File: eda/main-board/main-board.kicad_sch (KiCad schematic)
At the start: 11 parts, among them J3 Expansion, J4 $1-3 latch, J5 PWR, U1 W65C02SxP, X1 4Mhz

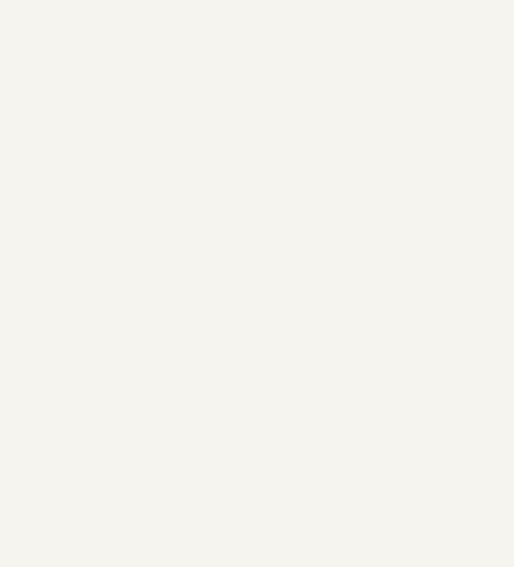
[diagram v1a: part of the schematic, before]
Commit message: Add expansion backplane
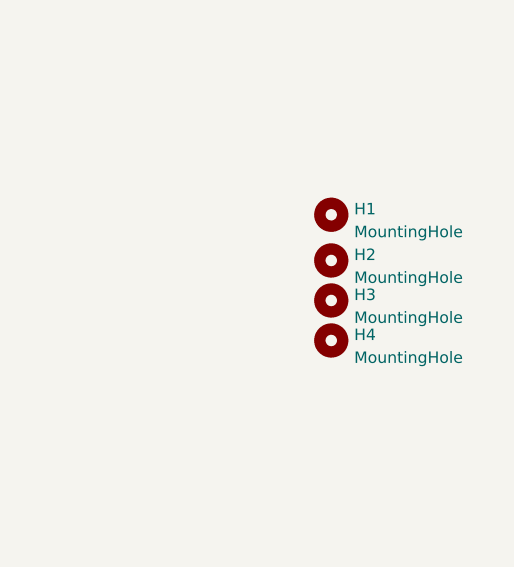
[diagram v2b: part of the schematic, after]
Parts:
- added H1, H2, H3, H4: MountingHole, MountingHole:MountingHole_2.1mm, symbol Mechanical:MountingHole
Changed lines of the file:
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@@
+    )
+  )
+  (symbol (lib_id "Mechanical:MountingHole") (at 267.97 137.16 0) (unit 1)
+    (in_bom yes) (on_board yes) (dnp no) (fields_autoplaced)
+    (property "Reference" "H1" (at 270.51 136.525 0)
+      (effects (font (size 1.27 1.27)) (justify left))
+    )
+    (property "Value" "MountingHole" (at 270.51 139.065 0)
+      (effects (font (size 1.27 1.27)) (justify left))
+    )
+    (property "Footprint" "MountingHole:MountingHole_2.1mm" (at 267.97 137.16 0)
+      (effects (font (size 1.27 1.27)) hide)
+    )
+    (property "Datasheet" "~" (at 267.97 137.16 0)
+      (effects (font (size 1.27 1.27)) hide)
+    )
+    (instances
+      (project "main-board"
+        (path "/2957ffac-6a43-4af7-8ab7-5cc1dbf2f2d7"
+          (reference "H1") (unit 1)
+        )
+      )
     )
   )
@@
     )
   )
+  (symbol (lib_id "Mechanical:MountingHole") (at 267.97 151.13 0) (unit 1)
+    (in_bom yes) (on_board yes) (dnp no) (fields_autoplaced)
+    (property "Reference" "H4" (at 270.51 150.495 0)
+      (effects (font (size 1.27 1.27)) (justify left))
+    )
+    (property "Value" "MountingHole" (at 270.51 153.035 0)
+      (effects (font (size 1.27 1.27)) (justify left))
+    )
+    (property "Footprint" "MountingHole:MountingHole_2.1mm" (at 267.97 151.13 0)
+      (effects (font (size 1.27 1.27)) hide)
+    )
+    (property "Datasheet" "~" (at 267.97 151.13 0)
+      (effects (font (size 1.27 1.27)) hide)
+    )
+    (instances
+      (project "main-board"
+        (path "/2957ffac-6a43-4af7-8ab7-5cc1dbf2f2d7"
+          (reference "H4") (unit 1)
+        )
+      )
+    )
+  )
   (symbol (lib_id "Device:R") (at 95.25 100.33 0) (unit 1)
     (in_bom yes) (on_board yes) (dnp no) (fields_autoplaced)
@@
     )
   )
+  (symbol (lib_id "Mechanical:MountingHole") (at 267.97 142.24 0) (unit 1)
+    (in_bom yes) (on_board yes) (dnp no) (fields_autoplaced)
+    (property "Reference" "H2" (at 270.51 141.605 0)
+      (effects (font (size 1.27 1.27)) (justify left))
+    )
+    (property "Value" "MountingHole" (at 270.51 144.145 0)
+      (effects (font (size 1.27 1.27)) (justify left))
+    )
+    (property "Footprint" "MountingHole:MountingHole_2.1mm" (at 267.97 142.24 0)
+      (effects (font (size 1.27 1.27)) hide)
+    )
+    (property "Datasheet" "~" (at 267.97 142.24 0)
+      (effects (font (size 1.27 1.27)) hide)
+    )
+    (instances
+      (project "main-board"
+        (path "/2957ffac-6a43-4af7-8ab7-5cc1dbf2f2d7"
+          (reference "H2") (unit 1)
+        )
+      )
+    )
+  )
   (symbol (lib_id "Device:R") (at 88.9 100.33 0) (unit 1)
     (in_bom yes) (on_board yes) (dnp no) (fields_autoplaced)
@@
         )
       )
+    )
+  )
+  (symbol (lib_id "Mechanical:MountingHole") (at 267.97 146.685 0) (unit 1)
+    (in_bom yes) (on_board yes) (dnp no) (fields_autoplaced)
+    (property "Reference" "H3" (at 270.51 146.05 0)
+      (effects (font (size 1.27 1.27)) (justify left))
+    )
+    (property "Value" "MountingHole" (at 270.51 148.59 0)
+      (effects (font (size 1.27 1.27)) (justify left))
+    )
+    (property "Footprint" "MountingHole:MountingHole_2.1mm" (at 267.97 146.685 0)
+      (effects (font (size 1.27 1.27)) hide)
+    )
+    (property "Datasheet" "~" (at 267.97 146.685 0)
+      (effects (font (size 1.27 1.27)) hide)
+    )
+    (instances
+      (project "main-board"
+        (path "/2957ffac-6a43-4af7-8ab7-5cc1dbf2f2d7"
+          (reference "H3") (unit 1)
+        )
+      )

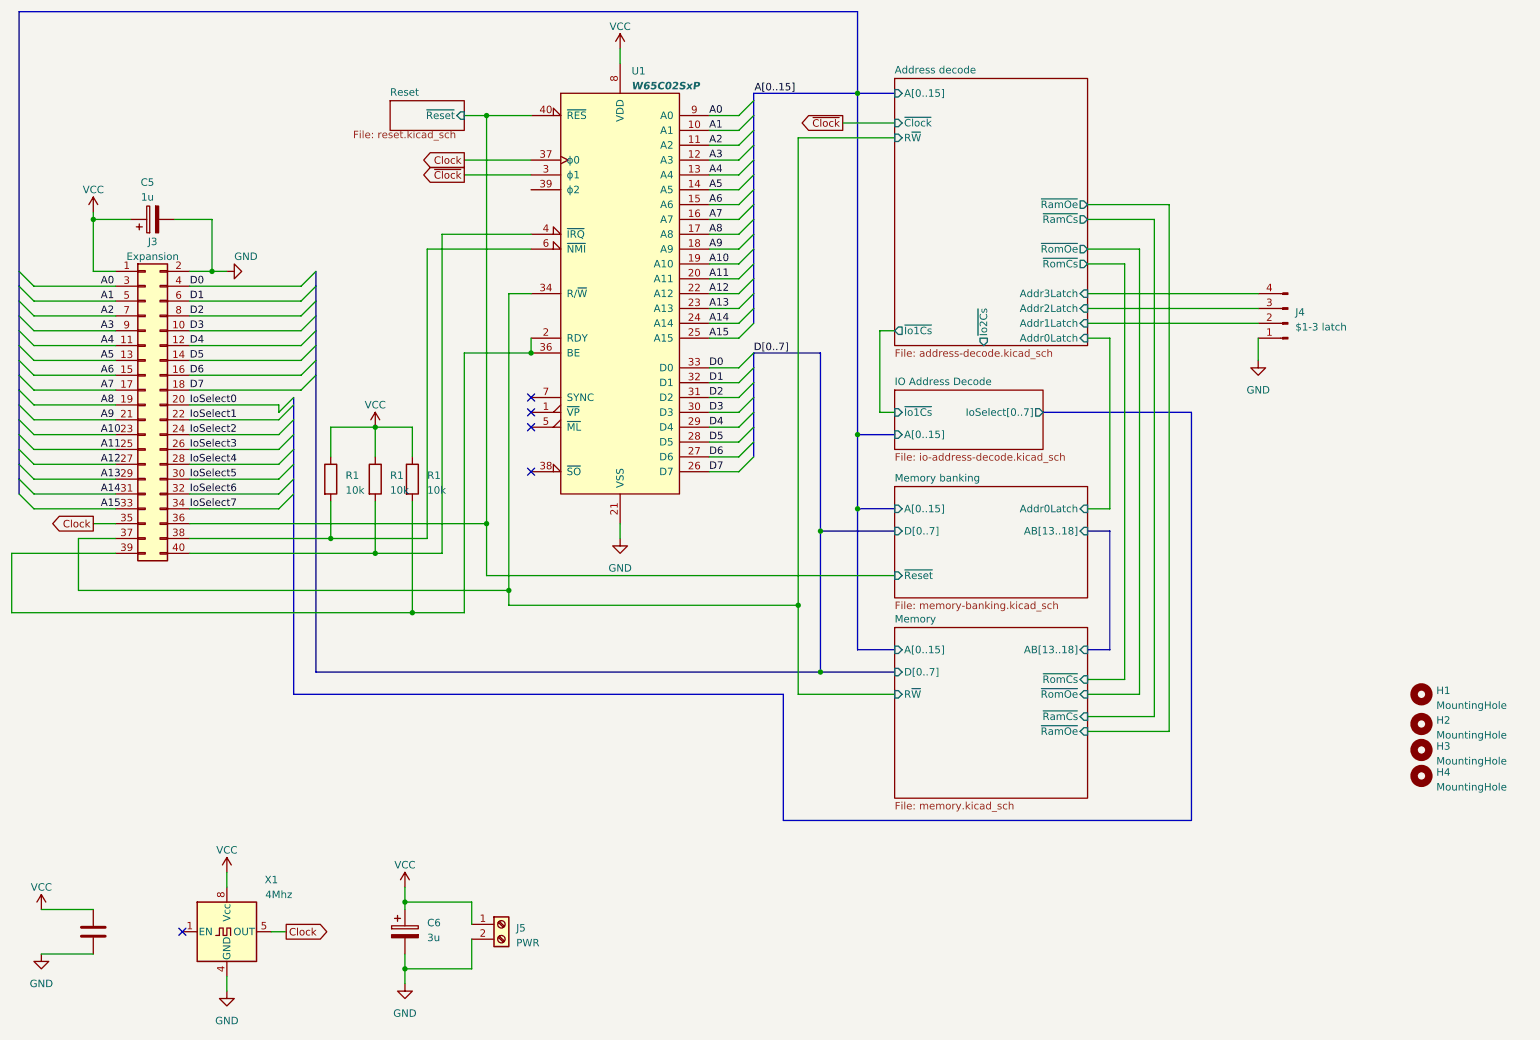
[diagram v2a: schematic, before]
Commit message: EDA work for new expansion header
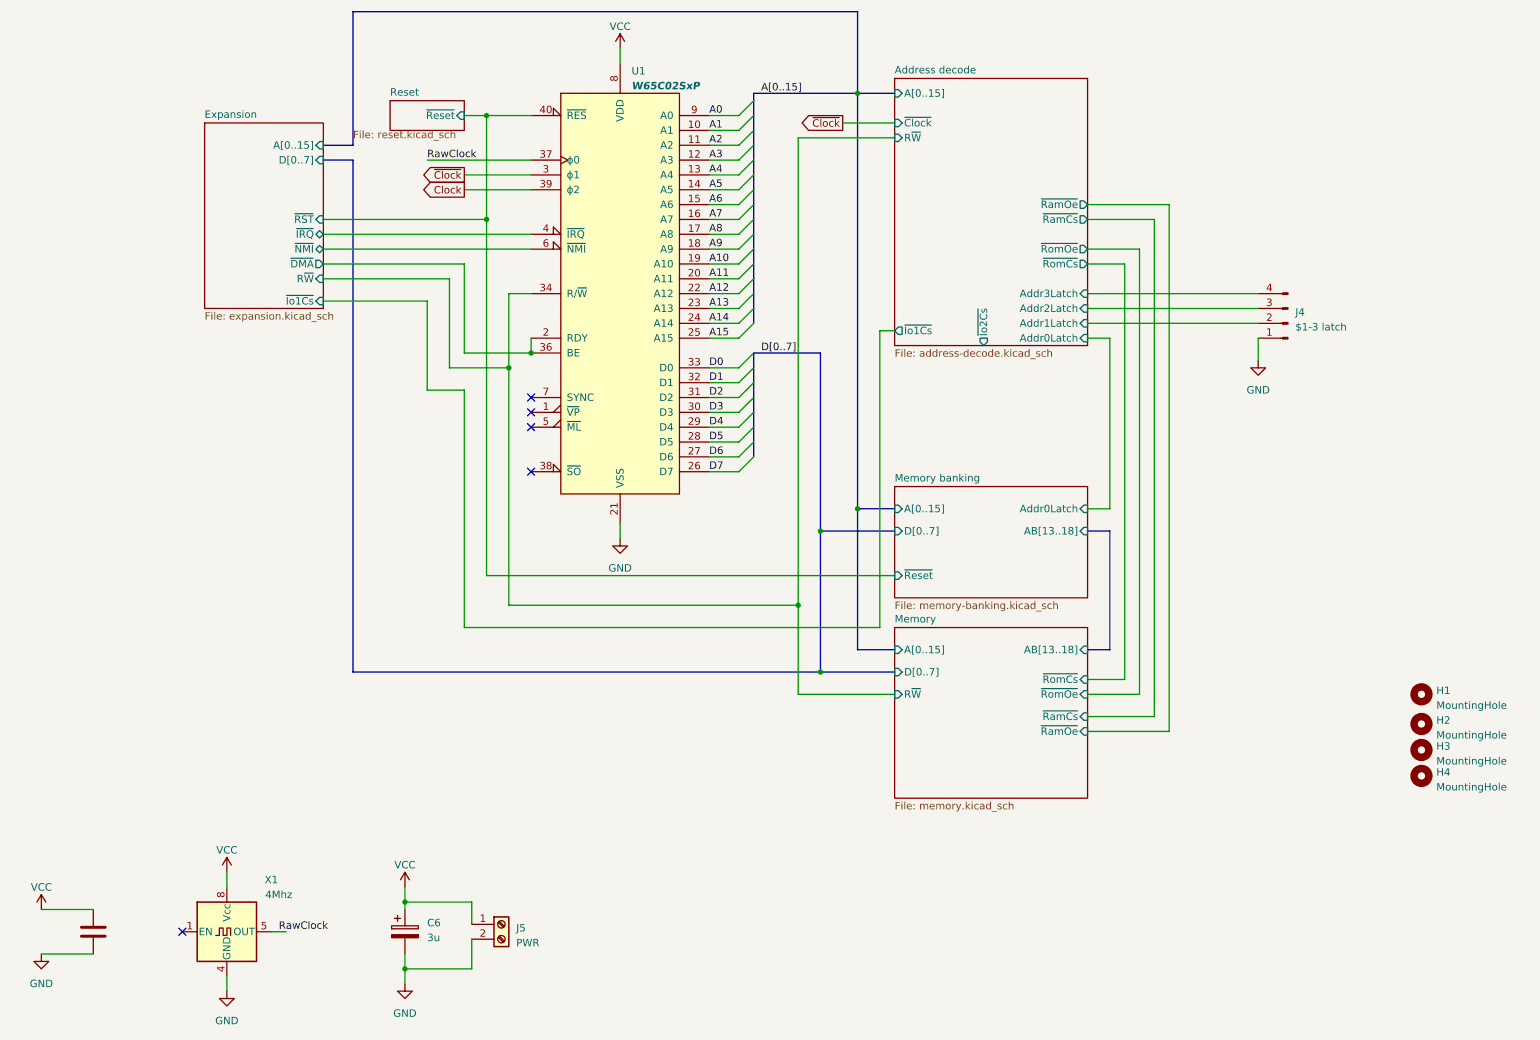
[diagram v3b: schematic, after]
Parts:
- removed C5: 1u, Capacitor_THT:CP_Radial_D8.0mm_P3.50mm, symbol Device:C_Polarized
- removed J3: Expansion, Connector_PinHeader_2.54mm:PinHeader_2x20_P2.54mm_Vertical, symbol Connector_Generic:Conn_02x20_Odd_Even
- removed R1 (x3): 10k, Resistor_THT:R_Axial_DIN0207_L6.3mm_D2.5mm_P7.62mm_Horizontal, symbol Device:R
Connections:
- net Clock: now also U1.39 (ϕ2); no longer U1.37 (ϕ0), X1.5 (OUT)
- net Expansion/~{DMA}: now reaches U1.2 (RDY), U1.36 (BE)
- net Expansion/~{IRQ}: now reaches U1.4 (~{IRQ})
- net Expansion/~{NMI}: now reaches U1.6 (~{NMI})
- net Memory banking/~{Reset} renamed Expansion/~{RST}
- new net RawClock: U1.37 (ϕ0), X1.5 (OUT)
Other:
- removed sheet IO Address Decode
- added sheet Expansion (expansion.kicad_sch)

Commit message: Branch of uart to v1
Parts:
- removed H1, H2, H3, H4: MountingHole, MountingHole:MountingHole_2.1mm, symbol Mechanical:MountingHole
- added D14: LED, LED_THT:LED_D3.0mm, symbol Device:LED
- added H1, H2, H3, H4, H5, H6: MountingHole_Pad, MountingHole:MountingHole_2.5mm_Pad_Via, symbol Mechanical:MountingHole_Pad
- added R1: 1k, Resistor_THT:R_Axial_DIN0207_L6.3mm_D2.5mm_P7.62mm_Horizontal, symbol Device:R
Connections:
- net GND: now also H1.1, H2.1, H3.1, H4.1, H5.1, H6.1, R1.2
- net VCC: now also D14.2 (A)
- new net: D14.1 (K), R1.1
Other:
- moved on the sheet: C6, J5

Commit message: Normalize cap size
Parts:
- C3: footprint Capacitor_THT:C_Disc_D6.0mm_W2.5mm_P5.00mm -> Capacitor_THT:C_Disc_D3.8mm_W2.6mm_P2.50mm
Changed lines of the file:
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@@
       (effects (font (size 1.27 1.27)) (justify left) hide)
     )
-    (property "Footprint" "Capacitor_THT:C_Disc_D6.0mm_W2.5mm_P5.00mm" (at 41.6052 181.61 0)
+    (property "Footprint" "Capacitor_THT:C_Disc_D3.8mm_W2.6mm_P2.50mm" (at 41.6052 181.61 0)
       (effects (font (size 1.27 1.27)) hide)
     )

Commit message: Rerouting IO card
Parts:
- renumbered C3 to C4, R1 to R10
